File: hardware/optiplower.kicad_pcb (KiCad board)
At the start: 2 copper layers, 68.8 x 17.2 mm, 22 parts, among them J1 Conn_01x02, J2 Conn_01x03, U1 DS2502S+, U2 XL4015, U3 ATtiny25-10SSU, U4 LR7533-M

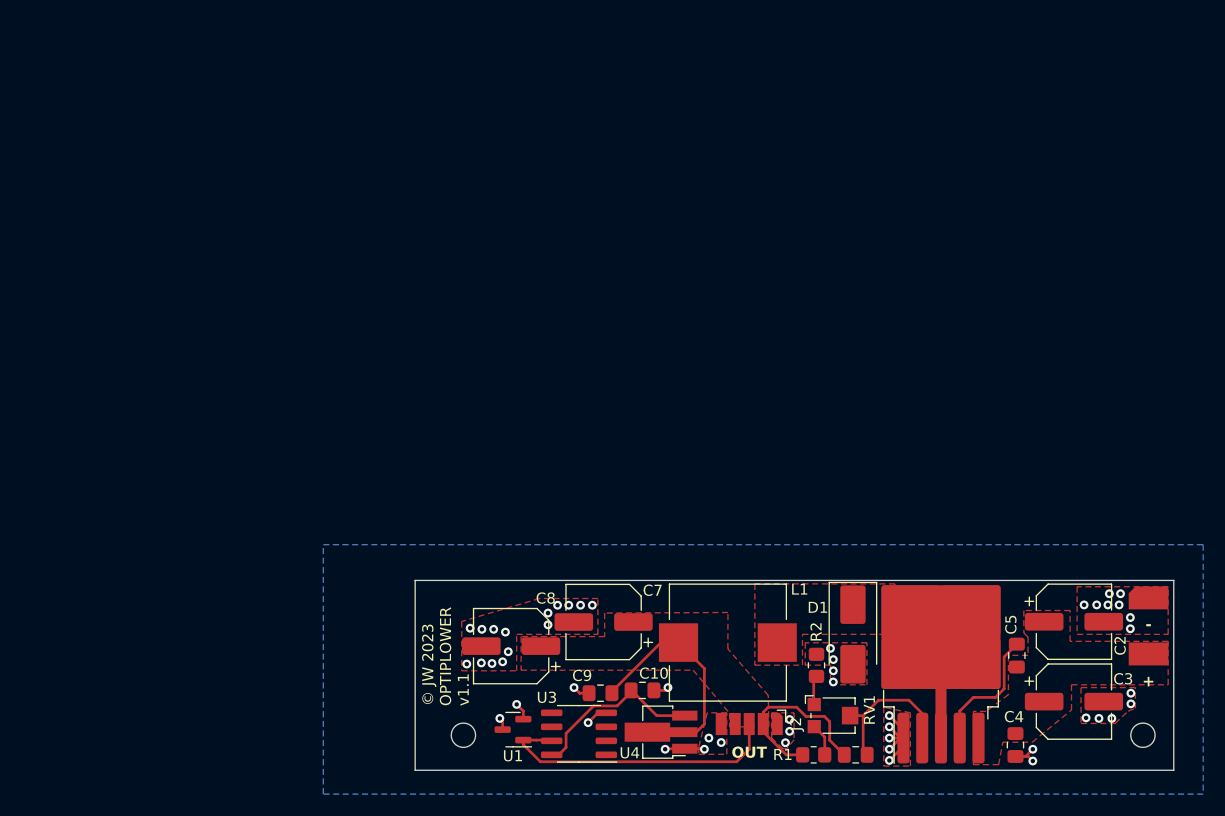
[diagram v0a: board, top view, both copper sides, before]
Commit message: Relayout so caps fit in gap
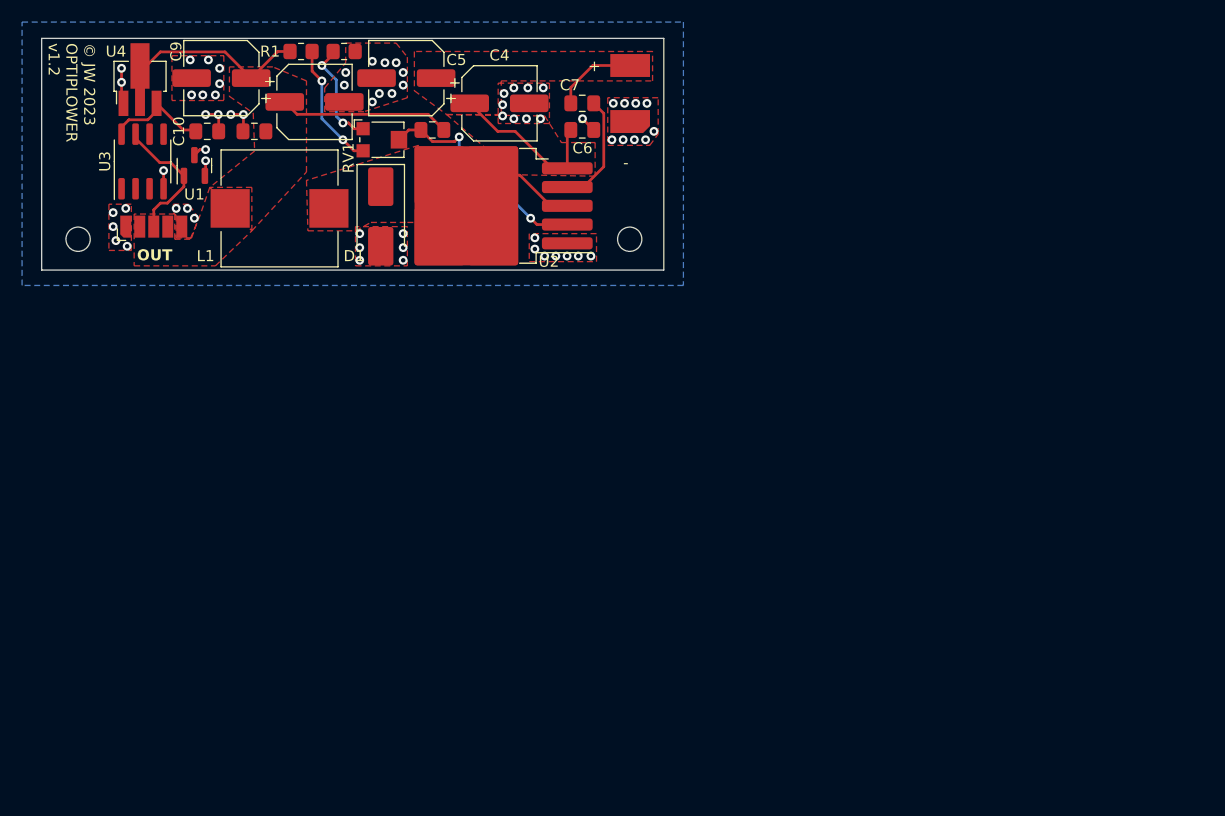
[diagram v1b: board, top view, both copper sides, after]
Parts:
- removed C2, C3: 220uF, Capacitor_SMD:CP_Elec_6.3x7.7
- added C11: 220uF, Capacitor_SMD:CP_Elec_6.3x7.7, F.Cu at (179.0, 35.1)
- added C12: 1uF, Capacitor_SMD:C_0805_2012Metric_Pad1.18x1.45mm_HandSolder, F.Cu at (173.6, 37.7)
- C4, C5, C9: value 1uF -> 220uF; footprint Capacitor_SMD:C_0805_2012Metric_Pad1.18x1.45mm_HandSolder -> Capacitor_SMD:CP_Elec_6.3x7.7
- C6: value 33n -> 1uF
- C7: value 220uF -> 1uF; footprint Capacitor_SMD:CP_Elec_6.3x7.7 -> Capacitor_SMD:C_0805_2012Metric_Pad1.18x1.45mm_HandSolder
- C8: value 220uF -> 33n; footprint Capacitor_SMD:CP_Elec_6.3x7.7 -> Capacitor_SMD:C_0805_2012Metric_Pad1.18x1.45mm_HandSolder
- moved R1 78.9 mm to (177.8, 30.5)
- moved C5 76.2 mm to (187.4, 32.9), turned to 180 degrees
- moved U4 75.7 mm to (163.2, 32.7), turned to 90 degrees
- moved C4 74.6 mm to (195.8, 35.2), turned to 0 degrees
- moved J2 74.3 mm to (161.9, 46.4), turned to 90 degrees
- moved J1 71.1 mm to (207.6, 31.8), turned to -90 degrees
- moved R2 70.2 mm to (181.7, 30.5), turned to 0 degrees
- moved RV1 66.3 mm to (185.2, 38.5)
- moved C9 65.5 mm to (170.6, 32.9)
- moved U3 65.2 mm to (163.4, 40.4), turned to 90 degrees
- moved H2 64.7 mm to (207.6, 47.5)
- moved C10 64.2 mm to (169.3, 37.7)
- moved C6 61.8 mm to (203.3, 37.6)
- moved U1 58.7 mm to (168.1, 40.8), turned to 90 degrees
- moved U2 58.1 mm to (194.3, 44.5), turned to 180 degrees
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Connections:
- C5 pad 2: Net-(U2-VC) -> GND
- C6 pad 1: VCC -> +24V
- C6 pad 2: Net-(U2-FB) -> GND
- C7 pad 1: VCC -> +24V
- C7 pad 2: GND -> Net-(U2-VC)
- C8 pad 2: GND -> Net-(U2-FB)
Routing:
- net +24V: track 0.00 -> 22.5 mm
- net /SENSE: track 26.9 -> 12.3 mm
- net GND: track 24.4 -> 14.3 mm, vias 51 -> 66
- net Net-(R1-Pad2): track 2.95 -> 11.4 mm, vias 0 -> 2
- net Net-(R2-Pad1): track 2.58 -> 9.73 mm, vias 0 -> 2
- net +3V3: track 16.3 -> 9.72 mm
- net Net-(U2-FB): track 13.5 -> 20.0 mm, vias 0 -> 2
- net Net-(U2-VC): track 11.8 -> 10.2 mm
- net /SW: track 9.15 -> 7.87 mm
- net VCC: track 35.1 -> 34.5 mm
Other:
- board size 68.8 x 17.2 mm -> 56.4 x 21 mm
- board text added: "© JW 2023 OPTIPLOWER v1.2"
- board text removed: "© JW 2023 OPTIPLOWER v1.1"
